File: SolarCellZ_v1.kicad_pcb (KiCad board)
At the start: 6 copper layers, 48.4 x 48.4 mm, 62 parts, among them IC1 TSL2561, J1 XF2M-1015-1A, Q1 IRLML2803, U1 NDS8434, U2 Value

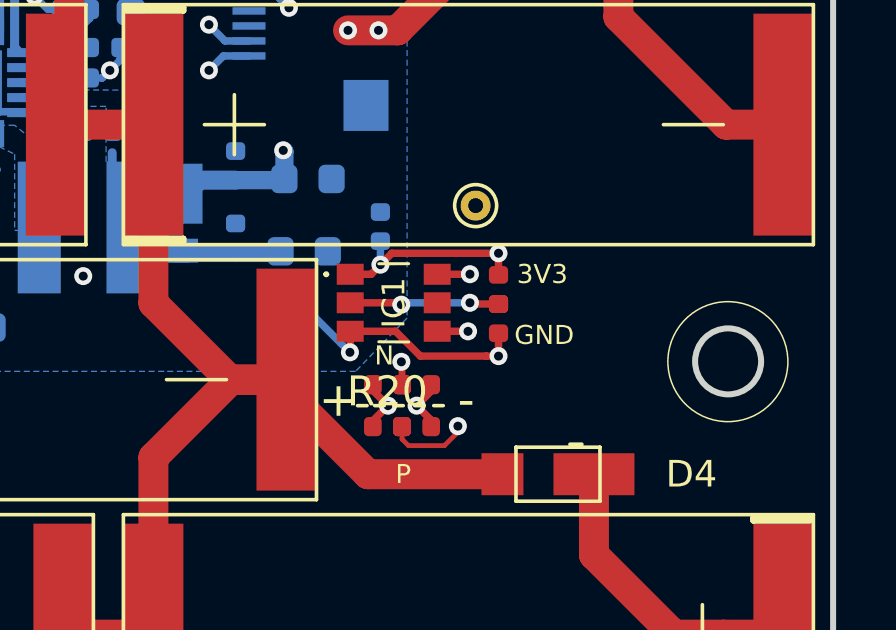
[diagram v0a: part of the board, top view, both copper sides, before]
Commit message: Modified magnetorquer coils
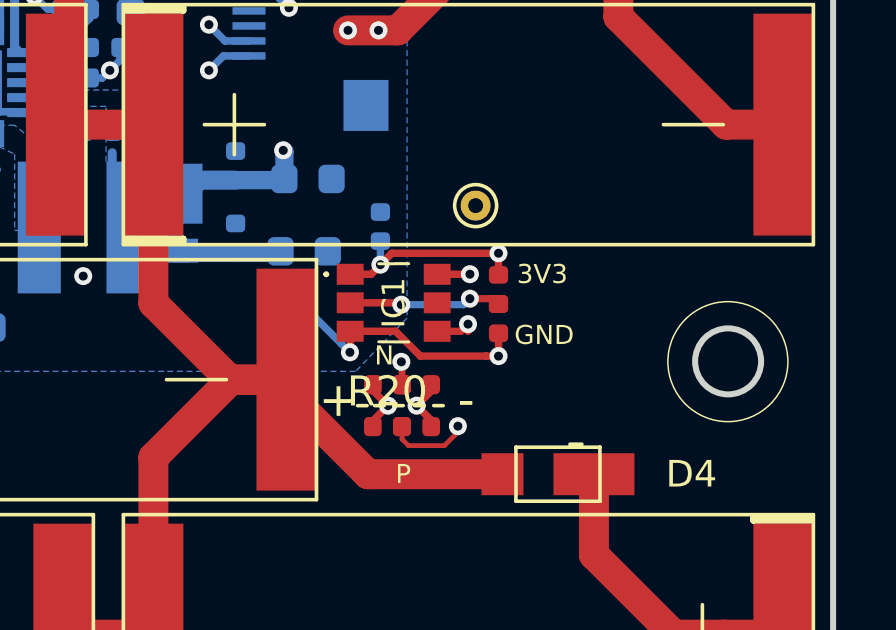
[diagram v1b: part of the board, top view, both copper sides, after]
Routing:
- net /coil: track 17150.8 -> 15795.0 mm

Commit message: design review and generated gerbers
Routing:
- net /coil: track 15795.0 -> 15793.7 mm
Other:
- rule pad_to_mask_clearance: 0.0508 -> 0.049
- rule solder_mask_min_width: 0.25 -> 0.099
- board text added: "1"
- board text added: "v02"
- board text removed: "v01"
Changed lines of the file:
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@@
-(kicad_pcb (version 20171130) (host pcbnew "(5.1.4-0-10_14)")
+(kicad_pcb (version 20171130) (host pcbnew 5.0.2-bee76a0~70~ubuntu18.04.1)
   (general
     (thickness 1.6)
-    (drawings 59)
-    (tracks 3131)
+    (drawings 60)
+    (tracks 3130)
     (zones 0)
     (modules 62)
@@
   (page A4)
   (layers
-    (0 Top signal hide)
-    (1 In1.Cu signal hide)
-    (2 In2.Cu signal hide)
-    (3 In3.Cu signal hide)
-    (4 In4.Cu signal)
-    (31 Bottom signal hide)
+    (0 Top signal)
+    (1 In1.Cu signal)
+    (2 In2.Cu signal)
+    (3 In3.Cu signal)
+    (4 In4.Cu signal hide)
+    (31 Bottom signal)
     (32 B.Adhes user hide)
     (33 F.Adhes user hide)
@@
     (35 F.Paste user hide)
     (36 B.SilkS user hide)
-    (37 F.SilkS user hide)
-    (38 B.Mask user hide)
+    (37 F.SilkS user)
+    (38 B.Mask user)
     (39 F.Mask user hide)
     (40 Dwgs.User user hide)
@@
   )
   (setup
-    (last_trace_width 0.48)
+    (last_trace_width 0.127)
     (user_trace_width 0.127)
     (user_trace_width 0.16)
@@
     (zone_45_only yes)
     (trace_min 0.127)
+    (segment_width 0.2)
+    (edge_width 0.05)
     (via_size 0.6)
     (via_drill 0.3)
@@
     (uvia_min_size 0.2)
     (uvia_min_drill 0.1)
-    (edge_width 0.05)
-    (segment_width 0.2)
     (pcb_text_width 0.3)
     (pcb_text_size 1.5 1.5)
@@
     (pad_size 1.524 1.524)
     (pad_drill 0.762)
-    (pad_to_mask_clearance 0.0508)
-    (solder_mask_min_width 0.25)
+    (pad_to_mask_clearance 0.049)
+    (solder_mask_min_width 0.099)
     (aux_axis_origin 0 0)
     (grid_origin 90 40)
     (visible_elements 7FFFF77F)
     (pcbplotparams
-      (layerselection 0x010f0_ffffffff)
+      (layerselection 0x010fc_ffffffff)
       (usegerberextensions false)
       (usegerberattributes true)
@@
     (uvia_dia 0.3)
     (uvia_drill 0.1)
-    (diff_pair_width 0.1524)
     (diff_pair_gap 0.1524)
+    (diff_pair_width 0.1524)
     (add_net +3V3)
     (add_net /VBAT)
@@
     )
   )
+  (gr_text 1 (at 120.45 55.2) (layer B.SilkS)
+    (effects (font (size 1.5 1.5) (thickness 0.3)) (justify mirror))
+  )
   (gr_circle (center 134.9075 73.391) (end 133.8075 73.391) (layer Edge.Cuts) (width 0.2))
   (gr_circle (center 95.1075 73.391) (end 94.0075 73.391) (layer Edge.Cuts) (width 0.2))
   (gr_line (start 103.4288 64.3128) (end 104.521 64.3128) (layer B.SilkS) (width 0.12))
-  (gr_text "Cable Pinout\n1.BATT_P\n2.BATT_N\n3.SDA\n4.SCL\n5.BURN\n6.3V3\n7.GND\n8.GND\n9.COIL_N\n10.COIL_P\n" (at 133.223 74.295) (layer B.SilkS)
+  (gr_text "Cable Pinout\n1.BATT_P\n2.BATT_N\n3.SDA\n4.SCL\n5.BURN\n6.3V3\n7.GND\n8.GND\n9.COIL_N\n10.COIL_P\n" (at 129.45 60.45) (layer B.SilkS)
     (effects (font (size 0.635 0.635) (thickness 0.0762)) (justify left mirror))
   )
@@
   (gr_line (start 107.4075 52.841) (end 107.4075 51.041) (layer Edge.Cuts) (width 0.2))
   (gr_line (start 99.2075 51.041) (end 99.2075 52.841) (layer Edge.Cuts) (width 0.2))
-  (gr_text BURN (at 122.936 55.3085) (layer B.SilkS)
+  (gr_text BURN (at 122.85 52.7) (layer B.SilkS)
     (effects (font (size 0.762 0.762) (thickness 0.1016)) (justify mirror))
   )
-  (gr_text BATT_P (at 116.459 55.3085) (layer B.SilkS)
+  (gr_text BATT_P (at 116.55 55.4) (layer B.SilkS)
     (effects (font (size 0.762 0.762) (thickness 0.1016)) (justify mirror))
   )
@@
     (effects (font (size 0.762 0.762) (thickness 0.1016)) (justify mirror))
   )
-  (gr_text v01 (at 135.1915 59.436) (layer B.Mask)
+  (gr_text v02 (at 135.1915 59.436) (layer B.Mask)
     (effects (font (size 1.5 1.5) (thickness 0.3)) (justify mirror))
   )
-  (gr_text v01 (at 135.1915 59.436) (layer Bottom)
+  (gr_text v02 (at 135.1915 59.436) (layer Bottom)
     (effects (font (size 1.5 1.5) (thickness 0.3)) (justify mirror))
   )
-  (gr_text v01 (at 135.4455 59.436) (layer F.Mask)
+  (gr_text v02 (at 135.4455 59.436) (layer F.Mask)
     (effects (font (size 1.5 1.5) (thickness 0.3)))
   )
-  (gr_text v01 (at 135.4455 59.436) (layer Top)
+  (gr_text v02 (at 135.4455 59.436) (layer Top)
     (effects (font (size 1.5 1.5) (thickness 0.3)))
   )
@@
   (segment (start 123.06822 74.168) (end 123.06822 74.36372) (width 0.24892) (layer Top) (net 29) (status 30))
   (segment (start 123.06822 75.36928) (end 123.571 74.8665) (width 0.24892) (layer Top) (net 29) (status 10))
-  (segment (start 123.952 75.438) (end 124.5235 74.8665) (width 0.127) (layer In4.Cu) (net 29))
-  (segment (start 101.981 64.516) (end 102.87 64.516) (width 0.127) (layer In4.Cu) (net 29))
-  (segment (start 100.33 66.167) (end 101.981 64.516) (width 0.127) (layer In4.Cu) (net 29))
-  (segment (start 122.8725 75.311) (end 122.9995 75.438) (width 0.127) (layer In4.Cu) (net 29))
-  (segment (start 102.87 64.516) (end 104.14 65.786) (width 0.127) (layer In4.Cu) (net 29))
-  (segment (start 122.9995 75.438) (end 123.952 75.438) (width 0.127) (layer In4.Cu) (net 29))
-  (segment (start 104.14 65.786) (end 104.14 71.882) (width 0.127) (layer In4.Cu) (net 29))
-  (segment (start 104.14 71.882) (end 107.569 75.311) (width 0.127) (layer In4.Cu) (net 29))
-  (segment (start 107.569 75.311) (end 122.8725 75.311) (width 0.127) (layer In4.Cu) (net 29))
-  (segment (start 101.981 64.262) (end 100.33 62.611) (width 0.127) (layer In4.Cu) (net 29))
-  (segment (start 123.3805 75.057) (end 107.696 75.057) (width 0.127) (layer In4.Cu) (net 29))
-  (segment (start 123.571 74.8665) (end 123.3805 75.057) (width 0.127) (layer In4.Cu) (net 29))
-  (segment (start 107.696 75.057) (end 104.394 71.755) (width 0.127) (layer In4.Cu) (net 29))
-  (segment (start 104.394 71.755) (end 104.394 65.659) (width 0.127) (layer In4.Cu) (net 29))
-  (segment (start 104.394 65.659) (end 102.997 64.262) (width 0.127) (layer In4.Cu) (net 29))
-  (segment (start 102.997 64.262) (end 101.981 64.262) (width 0.127) (layer In4.Cu) (net 29))
   (via (at 123.571 74.8665) (size 0.6) (drill 0.3) (layers Top Bottom) (net 29))
   (via (at 124.5235 74.8665) (size 0.6) (drill 0.3) (layers Top Bottom) (net 29))
@@
   (segment (start 91.7 62.1) (end 91.7 70.6) (width 0.19) (layer In3.Cu) (net 29))
   (segment (start 90.65 61.75) (end 90.65 71.65) (width 0.19) (layer In3.Cu) (net 29))
+  (segment (start 100.729999 63.010999) (end 102.810999 63.010999) (width 0.19) (layer In4.Cu) (net 29))
+  (segment (start 100.33 62.611) (end 100.729999 63.010999) (width 0.19) (layer In4.Cu) (net 29))
+  (segment (start 102.810999 63.010999) (end 104.65 64.85) (width 0.19) (layer In4.Cu) (net 29))
+  (segment (start 104.65 64.85) (end 104.65 71.75) (width 0.19) (layer In4.Cu) (net 29))
+  (segment (start 107.7665 74.8665) (end 123.571 74.8665) (width 0.19) (layer In4.Cu) (net 29))
+  (segment (start 104.65 71.75) (end 107.7665 74.8665) (width 0.19) (layer In4.Cu) (net 29))
+  (segment (start 123.1 75.6) (end 124.25 75.6) (width 0.19) (layer In4.Cu) (net 29))
+  (segment (start 103.217 66.167) (end 104.2 67.15) (width 0.19) (layer In4.Cu) (net 29))
+  (segment (start 124.5235 75.3265) (end 124.5235 74.8665) (width 0.19) (layer In4.Cu) (net 29))
+  (segment (start 104.2 67.15) (end 104.2 72.05) (width 0.19) (layer In4.Cu) (net 29))
+  (segment (start 104.2 72.05) (end 107.45 75.3) (width 0.19) (layer In4.Cu) (net 29))
+  (segment (start 124.25 75.6) (end 124.5235 75.3265) (width 0.19) (layer In4.Cu) (net 29))
+  (segment (start 100.33 66.167) (end 103.217 66.167) (width 0.19) (layer In4.Cu) (net 29))
+  (segment (start 107.45 75.3) (end 122.8 75.3) (width 0.19) (layer In4.Cu) (net 29))
+  (segment (start 122.8 75.3) (end 123.1 75.6) (width 0.19) (layer In4.Cu) (net 29))
   (segment (start 136.75 79.8) (end 136.75 82.5) (width 1) (layer Top) (net 30) (status 30))
   (segment (start 134.75 82.5) (end 136.75 82.5) (width 1) (layer Top) (net 30) (status 20))
@@
   )
   (zone (net 10) (net_name BATT_P) (layer Bottom) (hatch edge 0.508)
-    (connect_pads (clearance 0.127))
+    (connect_pads yes (clearance 0.127))
     (min_thickness 0.127)
     (fill yes (arc_segments 32) (thermal_gap 0.127) (thermal_bridge_width 0.1524))
@@
   )
   (zone (net 6) (net_name /VBURN) (layer Bottom) (hatch edge 0.508)
-    (connect_pads (clearance 0.127))
+    (connect_pads yes (clearance 0.127))
     (min_thickness 0.127)
     (fill yes (arc_segments 32) (thermal_gap 0.127) (thermal_bridge_width 0.1524))
